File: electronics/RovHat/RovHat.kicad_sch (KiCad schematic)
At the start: 0 parts

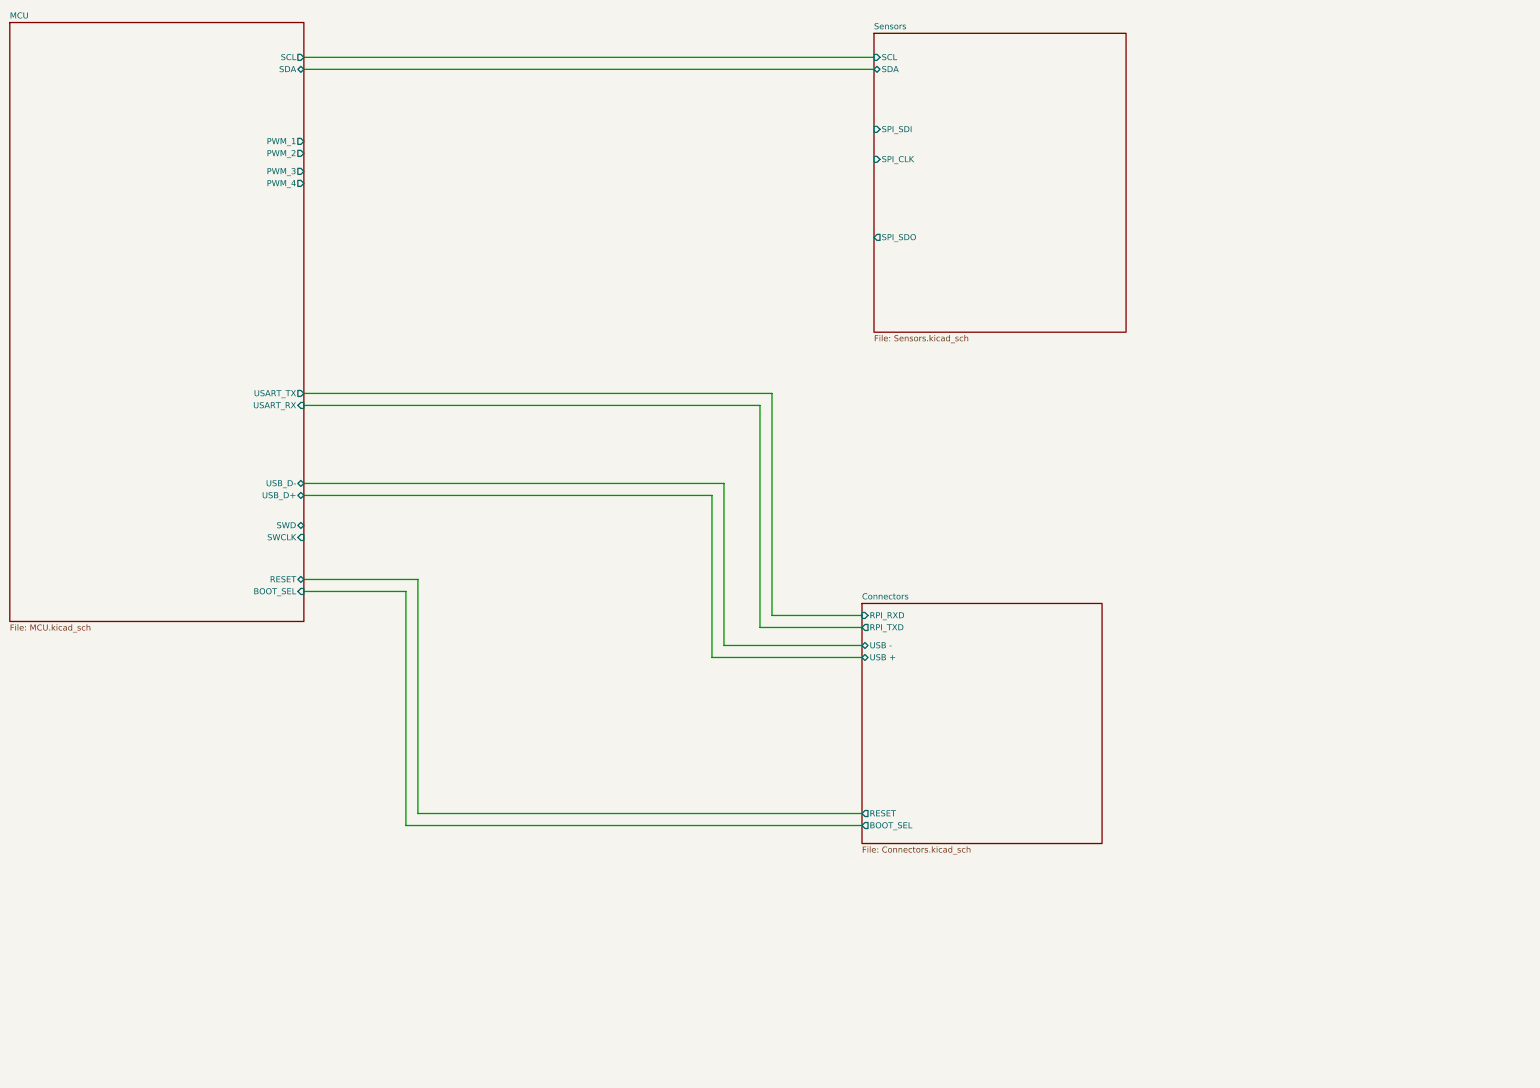
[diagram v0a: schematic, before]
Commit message: Changed To RPI Pico Module
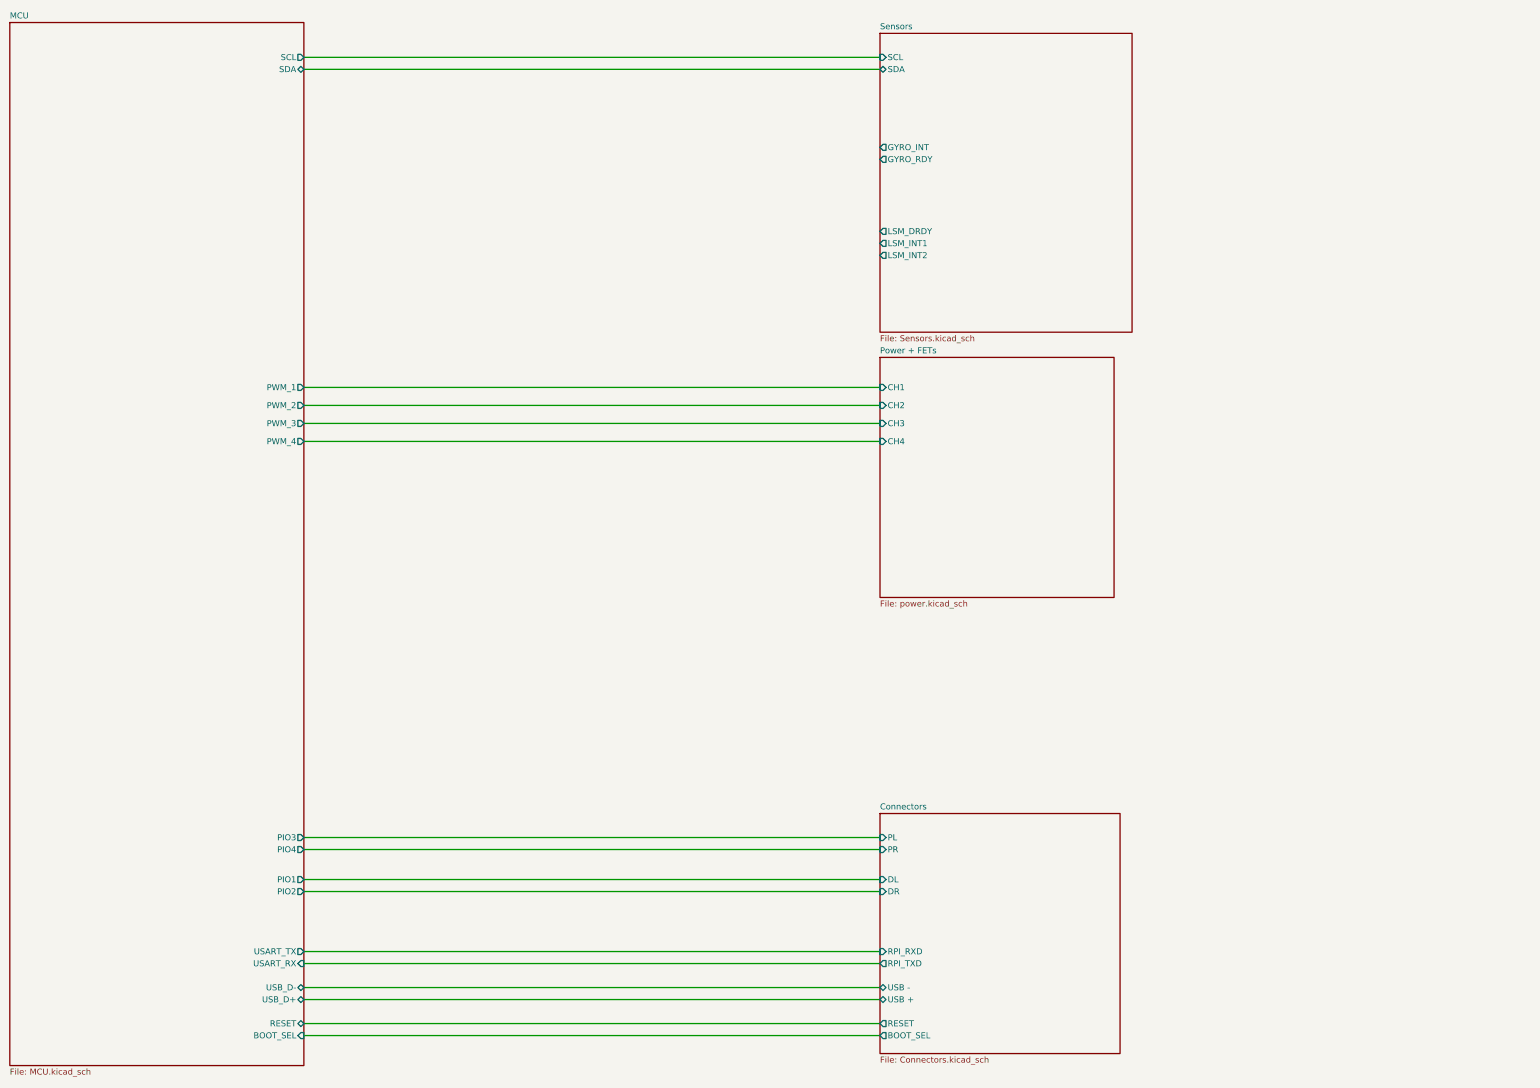
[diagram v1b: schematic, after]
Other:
- added sheet Power + FETs (power.kicad_sch)
- sheet Connectors ports: added DL, DR, PL, PR; removed none
- sheet MCU ports: added PIO1, PIO2, PIO3, PIO4; removed SWCLK, SWD
- sheet Sensors ports: added GYRO_INT, GYRO_RDY, LSM_DRDY, LSM_INT1, LSM_INT2; removed SPI_CLK, SPI_SDI, SPI_SDO

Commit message: Layout Done first level
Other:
- sheet MCU ports: added GYRO_INT, GYRO_RDY, LSM_DRDY, LSM_INT1, LSM_INT2; removed none
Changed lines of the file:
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@@
 (kicad_sch (version 20211123) (generator eeschema)
   (paper "A3")
+  (wire (pts (xy 144.78 54.61) (xy 266.7 54.61))
+    (stroke (width 0) (type default) (color 0 0 0 0))
+  )
   (wire (pts (xy 144.78 110.49) (xy 266.7 110.49))
     (stroke (width 0) (type default) (color 0 0 0 0))
   )
+  (wire (pts (xy 144.78 69.85) (xy 266.7 69.85))
+    (stroke (width 0) (type default) (color 0 0 0 0))
+  )
+  (wire (pts (xy 144.78 33.02) (xy 266.7 33.02))
+    (stroke (width 0) (type default) (color 0 0 0 0))
+  )
+  (wire (pts (xy 144.78 224.79) (xy 266.7 224.79))
+    (stroke (width 0) (type default) (color 0 0 0 0))
+  )
+  (wire (pts (xy 144.78 198.12) (xy 266.7 198.12))
+    (stroke (width 0) (type default) (color 0 0 0 0))
+  )
+  (wire (pts (xy 144.78 106.68) (xy 266.7 106.68))
+    (stroke (width 0) (type default) (color 0 0 0 0))
+  )
+  (wire (pts (xy 144.78 237.49) (xy 266.7 237.49))
+    (stroke (width 0) (type default) (color 0 0 0 0))
+  )
+  (wire (pts (xy 144.78 207.01) (xy 266.7 207.01))
+    (stroke (width 0) (type default) (color 0 0 0 0))
+  )
+  (wire (pts (xy 144.78 114.3) (xy 266.7 114.3))
+    (stroke (width 0) (type default) (color 0 0 0 0))
+  )
+  (wire (pts (xy 144.78 232.41) (xy 266.7 232.41))
+    (stroke (width 0) (type default) (color 0 0 0 0))
+  )
+  (wire (pts (xy 144.78 240.03) (xy 266.7 240.03))
+    (stroke (width 0) (type default) (color 0 0 0 0))
+  )
+  (wire (pts (xy 144.78 229.87) (xy 266.7 229.87))
+    (stroke (width 0) (type default) (color 0 0 0 0))
+  )
+  (wire (pts (xy 144.78 209.55) (xy 266.7 209.55))
+    (stroke (width 0) (type default) (color 0 0 0 0))
+  )
+  (wire (pts (xy 144.78 52.07) (xy 266.7 52.07))
+    (stroke (width 0) (type default) (color 0 0 0 0))
+  )
+  (wire (pts (xy 144.78 222.25) (xy 266.7 222.25))
+    (stroke (width 0) (type default) (color 0 0 0 0))
+  )
+  (wire (pts (xy 144.78 72.39) (xy 266.7 72.39))
+    (stroke (width 0) (type default) (color 0 0 0 0))
+  )
+  (wire (pts (xy 144.78 74.93) (xy 266.7 74.93))
+    (stroke (width 0) (type default) (color 0 0 0 0))
+  )
   (wire (pts (xy 144.78 102.87) (xy 266.7 102.87))
     (stroke (width 0) (type default) (color 0 0 0 0))
   )
-  (wire (pts (xy 144.78 33.02) (xy 266.7 33.02))
-    (stroke (width 0) (type default) (color 0 0 0 0))
-  )
-  (wire (pts (xy 144.78 224.79) (xy 266.7 224.79))
-    (stroke (width 0) (type default) (color 0 0 0 0))
-  )
-  (wire (pts (xy 144.78 198.12) (xy 266.7 198.12))
-    (stroke (width 0) (type default) (color 0 0 0 0))
-  )
-  (wire (pts (xy 144.78 237.49) (xy 266.7 237.49))
-    (stroke (width 0) (type default) (color 0 0 0 0))
-  )
-  (wire (pts (xy 144.78 207.01) (xy 266.7 207.01))
-    (stroke (width 0) (type default) (color 0 0 0 0))
-  )
-  (wire (pts (xy 144.78 114.3) (xy 266.7 114.3))
-    (stroke (width 0) (type default) (color 0 0 0 0))
-  )
-  (wire (pts (xy 144.78 232.41) (xy 266.7 232.41))
-    (stroke (width 0) (type default) (color 0 0 0 0))
-  )
-  (wire (pts (xy 144.78 240.03) (xy 266.7 240.03))
-    (stroke (width 0) (type default) (color 0 0 0 0))
-  )
-  (wire (pts (xy 144.78 229.87) (xy 266.7 229.87))
-    (stroke (width 0) (type default) (color 0 0 0 0))
-  )
-  (wire (pts (xy 144.78 209.55) (xy 266.7 209.55))
-    (stroke (width 0) (type default) (color 0 0 0 0))
-  )
-  (wire (pts (xy 144.78 222.25) (xy 266.7 222.25))
-    (stroke (width 0) (type default) (color 0 0 0 0))
-  )
   (wire (pts (xy 144.78 35.56) (xy 266.7 35.56))
-    (stroke (width 0) (type default) (color 0 0 0 0))
-  )
-  (wire (pts (xy 144.78 106.68) (xy 266.7 106.68))
     (stroke (width 0) (type default) (color 0 0 0 0))
   )
@@
     )
     (pin "PIO2" output (at 144.78 209.55 0)
+      (effects (font (size 1.27 1.27)) (justify right))
+    )
+    (pin "GYRO_INT" input (at 144.78 52.07 0)
+      (effects (font (size 1.27 1.27)) (justify right))
+    )
+    (pin "GYRO_RDY" input (at 144.78 54.61 0)
+      (effects (font (size 1.27 1.27)) (justify right))
+    )
+    (pin "LSM_INT1" input (at 144.78 72.39 0)
+      (effects (font (size 1.27 1.27)) (justify right))
+    )
+    (pin "LSM_INT2" input (at 144.78 74.93 0)
+      (effects (font (size 1.27 1.27)) (justify right))
+    )
+    (pin "LSM_DRDY" input (at 144.78 69.85 0)
       (effects (font (size 1.27 1.27)) (justify right))
     )
@@
   )
   (symbol_instances
+    (path "/212ae4ce-78ca-42fb-a0a9-9e7afe94e4f9/876ab51d-81be-4e3d-b934-e8be2b045c4e"
+      (reference "#FLG0101") (unit 1) (value "PWR_FLAG") (footprint "")
+    )
+    (path "/212ae4ce-78ca-42fb-a0a9-9e7afe94e4f9/16f162da-8b96-4f73-bec1-c68ccf6536d2"
+      (reference "#FLG0102") (unit 1) (value "PWR_FLAG") (footprint "")
+    )
+    (path "/212ae4ce-78ca-42fb-a0a9-9e7afe94e4f9/bee78a0b-b1cf-4707-bdbc-2bd42ad9eb21"
+      (reference "#FLG0103") (unit 1) (value "PWR_FLAG") (footprint "")
+    )
+    (path "/ac5eb4a7-a387-48d6-b4f5-8a76d938534b/19cd669a-4c1b-473a-b3f0-d9f48828f632"
+      (reference "#FLG0104") (unit 1) (value "PWR_FLAG") (footprint "")
+    )
     (path "/ac5eb4a7-a387-48d6-b4f5-8a76d938534b/37a1b69b-8bd0-4989-8b0a-8868e66416a5"
       (reference "#PWR0101") (unit 1) (value "+3.3VA") (footprint "")
@@
       (reference "#PWR0126") (unit 1) (value "GND") (footprint "")
     )
+    (path "/0a21e7d0-6c69-4634-b2b6-f0d0223d8049/bc3bab5c-4d1d-47c7-88e9-f5645e7f1544"
+      (reference "#PWR0127") (unit 1) (value "VDD") (footprint "")
+    )
+    (path "/0a21e7d0-6c69-4634-b2b6-f0d0223d8049/9cd43f82-bca8-4474-8b55-b123aeef9451"
+      (reference "#PWR0128") (unit 1) (value "VBUS") (footprint "")
+    )
+    (path "/d0328239-535b-4cf1-98be-6519c44fecfc/e8bad306-590e-48ff-bf55-31e89f1f285f"
+      (reference "#PWR0129") (unit 1) (value "VBUS") (footprint "")
+    )
     (path "/ac5eb4a7-a387-48d6-b4f5-8a76d938534b/2ed2429b-3346-4e05-a839-5c69e0f0f9d8"
       (reference "#PWR0201") (unit 1) (value "+3.3VA") (footprint "")
@@
       (reference "#PWR0403") (unit 1) (value "+5V") (footprint "")
     )
-    (path "/d0328239-535b-4cf1-98be-6519c44fecfc/f13d04c4-5914-4d23-8a71-cbec21f1f73d"
-      (reference "#PWR0404") (unit 1) (value "+5V") (footprint "")
-    )
     (path "/d0328239-535b-4cf1-98be-6519c44fecfc/fdb6c8aa-df0f-40d5-92a0-d50969af0525"
       (reference "#PWR0405") (unit 1) (value "GND") (footprint "")
@@
       (reference "#PWR0502") (unit 1) (value "GND") (footprint "")
     )
-    (path "/0a21e7d0-6c69-4634-b2b6-f0d0223d8049/bc3bab5c-4d1d-47c7-88e9-f5645e7f1544"
-      (reference "#PWR?") (unit 1) (value "VDD") (footprint "")
-    )
     (path "/ac5eb4a7-a387-48d6-b4f5-8a76d938534b/31476c52-21e0-4b78-b5b3-f6e0efc129b3"
       (reference "C201") (unit 1) (value "1u") (footprint "Capacitor_SMD:C_0402_1005Metric")
@@
     )
     (path "/d0328239-535b-4cf1-98be-6519c44fecfc/e8954d33-84e9-41ff-aedf-5c767fc88f72"
-      (reference "J401") (unit 1) (value "Conn_02x20_Odd_Even") (footprint "Connector_PinHeader_2.54mm:PinHeader_2x20_P2.54mm_Vertical")
+      (reference "J401") (unit 1) (value "RPI Header") (footprint "Connector_PinHeader_2.54mm:PinHeader_2x20_P2.54mm_Vertical")
     )
     (path "/d0328239-535b-4cf1-98be-6519c44fecfc/f7ab5944-0411-4048-a2ab-be8718298516"
@@
       (reference "J507") (unit 1) (value "PWR OUT") (footprint "Connector_PinHeader_2.54mm:PinHeader_1x02_P2.54mm_Vertical")
     )
-    (path "/212ae4ce-78ca-42fb-a0a9-9e7afe94e4f9/32f67a99-9c13-4799-849f-2cdc03df9742"
-      (reference "Q501") (unit 1) (value "AOD508") (footprint "Package_TO_SOT_SMD:TO-252-2")
-    )
-    (path "/212ae4ce-78ca-42fb-a0a9-9e7afe94e4f9/3bfbba7f-55a2-4bbc-a31f-e94f39248b5d"
-      (reference "Q502") (unit 1) (value "AOD508") (footprint "Package_TO_SOT_SMD:TO-252-2")
-    )
-    (path "/212ae4ce-78ca-42fb-a0a9-9e7afe94e4f9/476fa25b-0bf9-487e-9dad-f4add718d509"
-      (reference "Q503") (unit 1) (value "AOD508") (footprint "Package_TO_SOT_SMD:TO-252-2")
-    )
-    (path "/212ae4ce-78ca-42fb-a0a9-9e7afe94e4f9/f6d28249-55c4-4d5b-82c8-839b2d43f77b"
-      (reference "Q504") (unit 1) (value "AOD508") (footprint "Package_TO_SOT_SMD:TO-252-2")
+    (path "/212ae4ce-78ca-42fb-a0a9-9e7afe94e4f9/ea3205bd-63c2-4b68-8f79-e7d557f0c3ea"
+      (reference "Q501") (unit 1) (value "IRF7403") (footprint "Package_SO:SOIC-8_3.9x4.9mm_P1.27mm")
+    )
+    (path "/212ae4ce-78ca-42fb-a0a9-9e7afe94e4f9/da167ad0-83e8-440a-a12a-70db82e3c6f7"
+      (reference "Q502") (unit 1) (value "IRF7403") (footprint "Package_SO:SOIC-8_3.9x4.9mm_P1.27mm")
+    )
+    (path "/212ae4ce-78ca-42fb-a0a9-9e7afe94e4f9/1b93ccbd-d7c1-4b24-920c-d08b82d3acd2"
+      (reference "Q503") (unit 1) (value "IRF7403") (footprint "Package_SO:SOIC-8_3.9x4.9mm_P1.27mm")
+    )
+    (path "/212ae4ce-78ca-42fb-a0a9-9e7afe94e4f9/1038bc53-99de-4b70-8cfd-480964829b95"
+      (reference "Q504") (unit 1) (value "IRF7403") (footprint "Package_SO:SOIC-8_3.9x4.9mm_P1.27mm")
     )
     (path "/ac5eb4a7-a387-48d6-b4f5-8a76d938534b/547be16a-156b-4fb7-9944-5b8f99ecfb33"
